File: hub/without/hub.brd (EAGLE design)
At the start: 28.2 x 25.4 mm, 5 parts

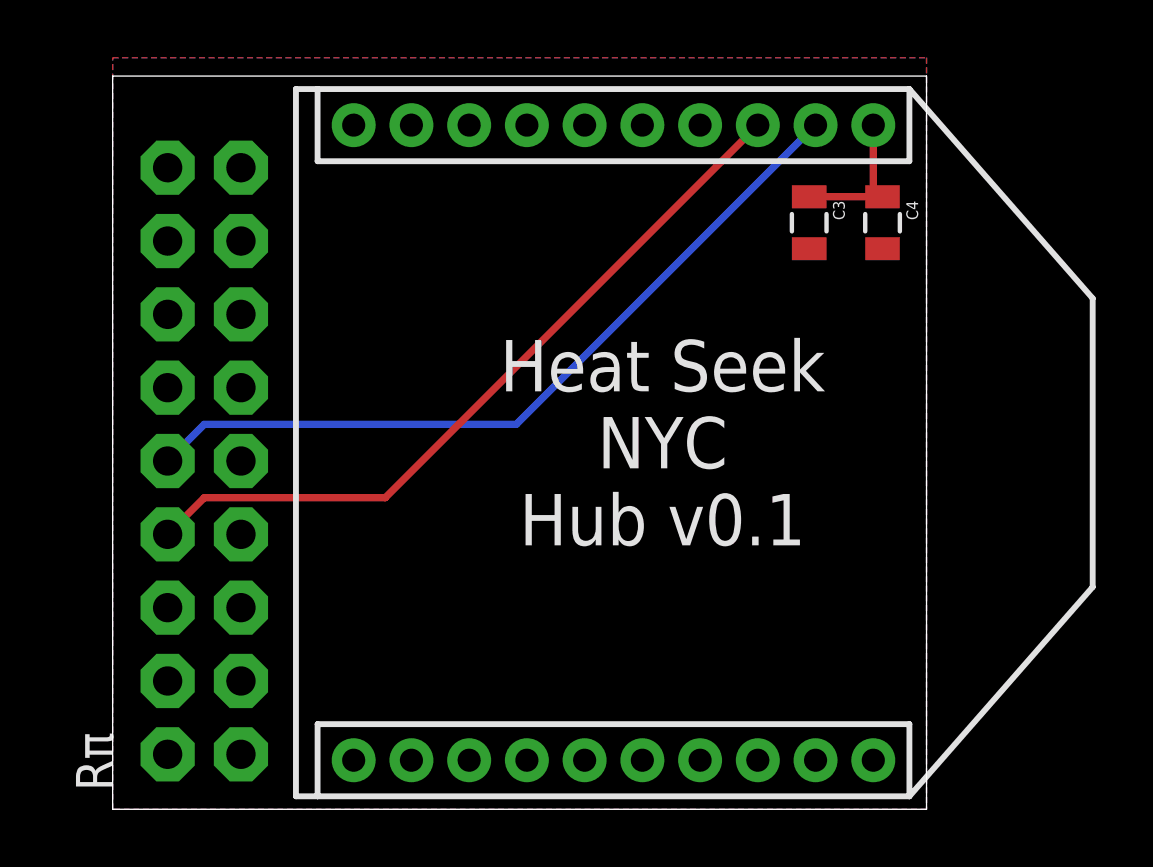
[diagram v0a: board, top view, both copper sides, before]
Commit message: tighter fit, turns out XBee fits perfectly on 1" wide board
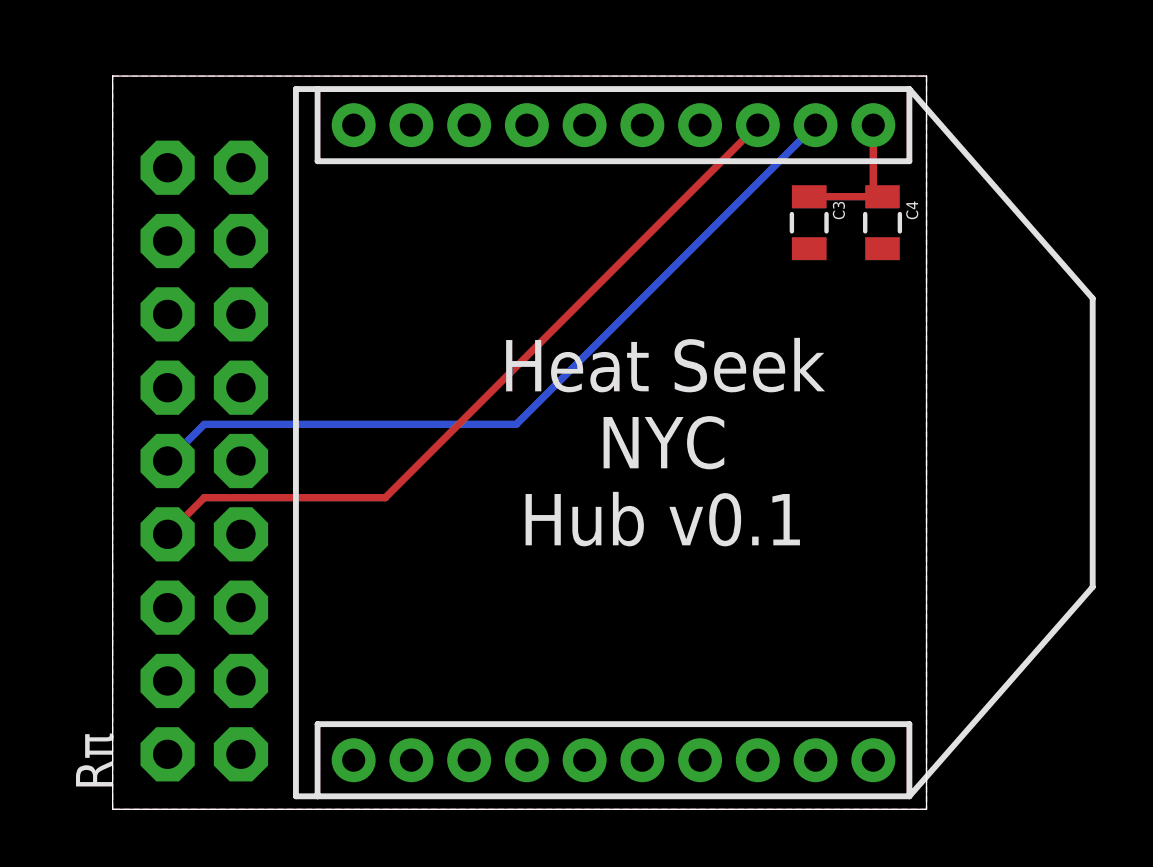
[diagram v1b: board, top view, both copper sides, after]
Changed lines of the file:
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@@
 <polygon width="0.3048" layer="1" isolate="0.3048">
 <vertex x="0" y="0"/>
-<vertex x="0" y="26.035"/>
-<vertex x="28.194" y="26.035"/>
+<vertex x="0" y="25.4"/>
+<vertex x="28.194" y="25.4"/>
 <vertex x="28.194" y="0"/>
 </polygon>
@@
 <polygon width="0.3048" layer="16" isolate="0.3048">
 <vertex x="0" y="0"/>
-<vertex x="0" y="26.035"/>
-<vertex x="28.194" y="26.035"/>
+<vertex x="0" y="25.4"/>
+<vertex x="28.194" y="25.4"/>
 <vertex x="28.194" y="0"/>
 </polygon>

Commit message: rename chips
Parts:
- renumbered C3 to C1, C4 to C2
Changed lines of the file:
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@@
 <element name="Rπ" library="hrldcpr" package="2X9_NOSILK" value="M9X2" x="3.175" y="12.065" rot="R90"/>
 <element name="XB24" library="hrldcpr" package="XBEE-1" value="XBEE-1XBEE-1" x="6.35" y="12.7" rot="R270"/>
-<element name="C3" library="SparkFun-Capacitors" package="0805" value="1µF" x="24.13" y="20.32" rot="R270"/>
-<element name="C4" library="SparkFun-Capacitors" package="0805" value="8.2pF" x="26.67" y="20.32" rot="R270"/>
+<element name="C1" library="SparkFun-Capacitors" package="0805" value="1µF" x="24.13" y="20.32" rot="R270"/>
+<element name="C2" library="SparkFun-Capacitors" package="0805" value="8.2pF" x="26.67" y="20.32" rot="R270"/>
 </elements>
 <signals>
@@
 <contactref element="Rπ" pad="9"/>
 <contactref element="Rπ" pad="6"/>
-<contactref element="C3" pad="2"/>
-<contactref element="C4" pad="2"/>
+<contactref element="C1" pad="2"/>
+<contactref element="C2" pad="2"/>
 <contactref element="XB24" pad="10"/>
 <polygon width="0.3048" layer="1" isolate="0.3048">
@@
 </polygon>
 <contactref element="Rπ" pad="1"/>
-<contactref element="C3" pad="1"/>
-<contactref element="C4" pad="1"/>
+<contactref element="C1" pad="1"/>
+<contactref element="C2" pad="1"/>
 <contactref element="XB24" pad="1"/>
 <wire x1="24.13" y1="21.22" x2="26.67" y2="21.22" width="0.254" layer="1"/>
